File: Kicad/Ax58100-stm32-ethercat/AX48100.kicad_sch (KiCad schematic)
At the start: 33 parts, among them U2 AX58100, U3 24LC32A, Y1 NXK25.000AE12F-KAB6-12

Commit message: Steppers, encoders, IO, etc remapped
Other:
- title: (none) -> MetalMusings EaserCAT 3000
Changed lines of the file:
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@@
 (kicad_sch (version 20230121) (generator eeschema)
   (paper "A4")
+  (title_block
+    (title "MetalMusings EaserCAT 3000")
+  )
   (junction (at 236.22 125.73) (diameter 0) (color 0 0 0 0)
   )

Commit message: wip
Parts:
- renumbered C33 to C18, C31 to C19, C30 to C20, C29 to C21, C28 to C22, C27 to C23, C26 to C34, C25 to C35, C24 to C36, C23 to C37, C13 to C42, C18 to C43, C17 to C44, C16 to C45, C15 to C46, C14 to C47, C12 to C48, C11 to C49, R40 to R23, R39 to R24, R38 to R25, R37 to R26, R31 to R37, R30 to R38, R26 to R44, R25 to R45, R24 to R46, R23 to R47, R21 to R48, U2 to U11, U3 to U9, Y1 to Y2

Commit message: Might be in final shape.
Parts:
- renumbered C22 to C16, C34 to C20, C36 to C21, C18 to C22, C19 to C23, C20 to C24, C21 to C25, C23 to C27, C35 to C39, C37 to C40, C42 to C45, C43 to C46, C44 to C47, C45 to C48, C46 to C49, C47 to C50, C48 to C51, C49 to C52, R26 to R41, R38 to R42, R25 to R43, R24 to R44, R23 to R46, R37 to R57, R44 to R64, R45 to R65, R46 to R66, R47 to R67, R48 to R68, U11 to U10, U9 to U8

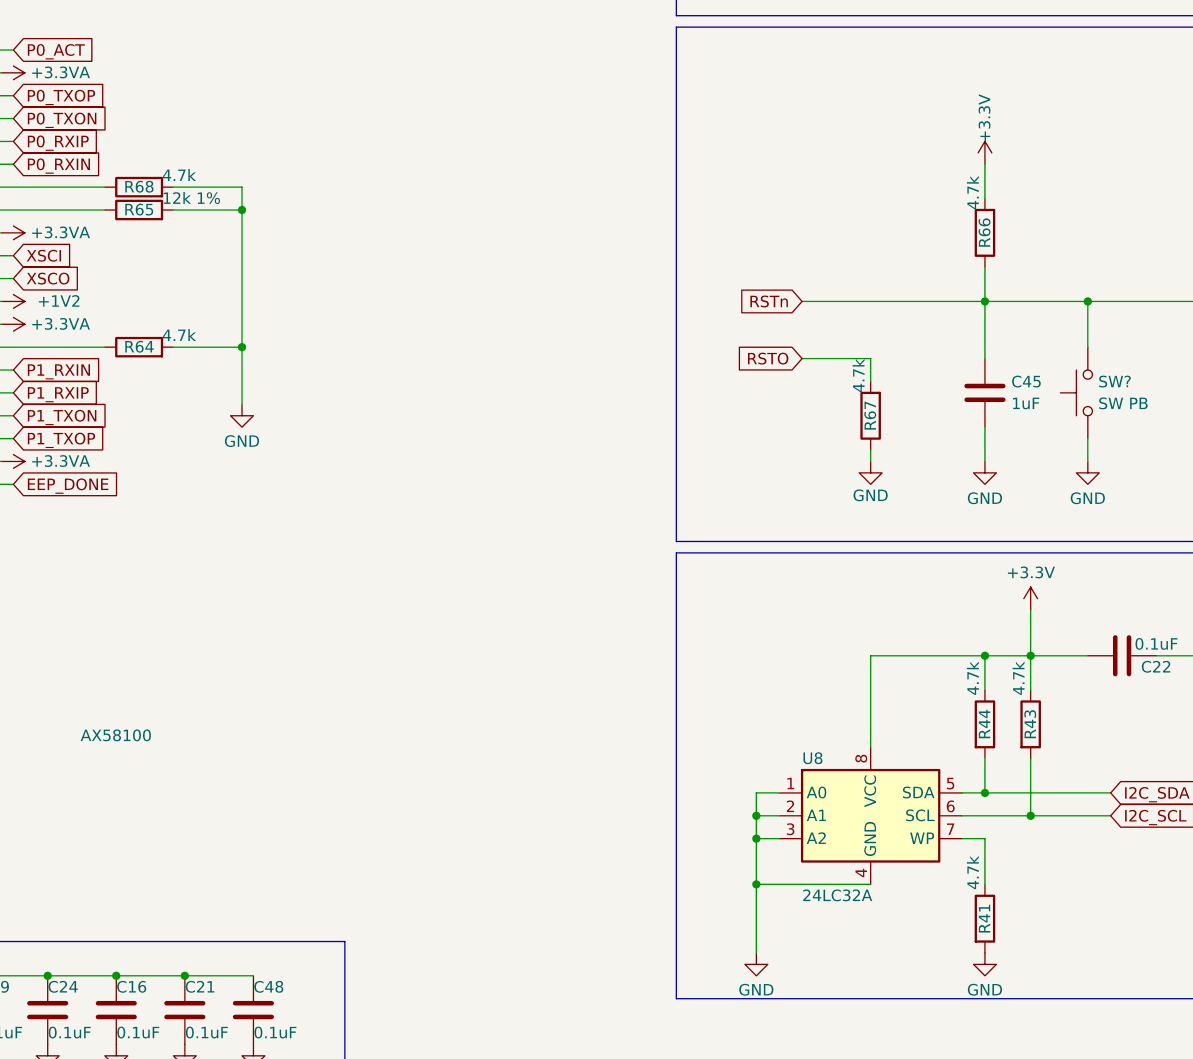
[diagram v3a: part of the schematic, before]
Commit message: 4.7k to 4k7
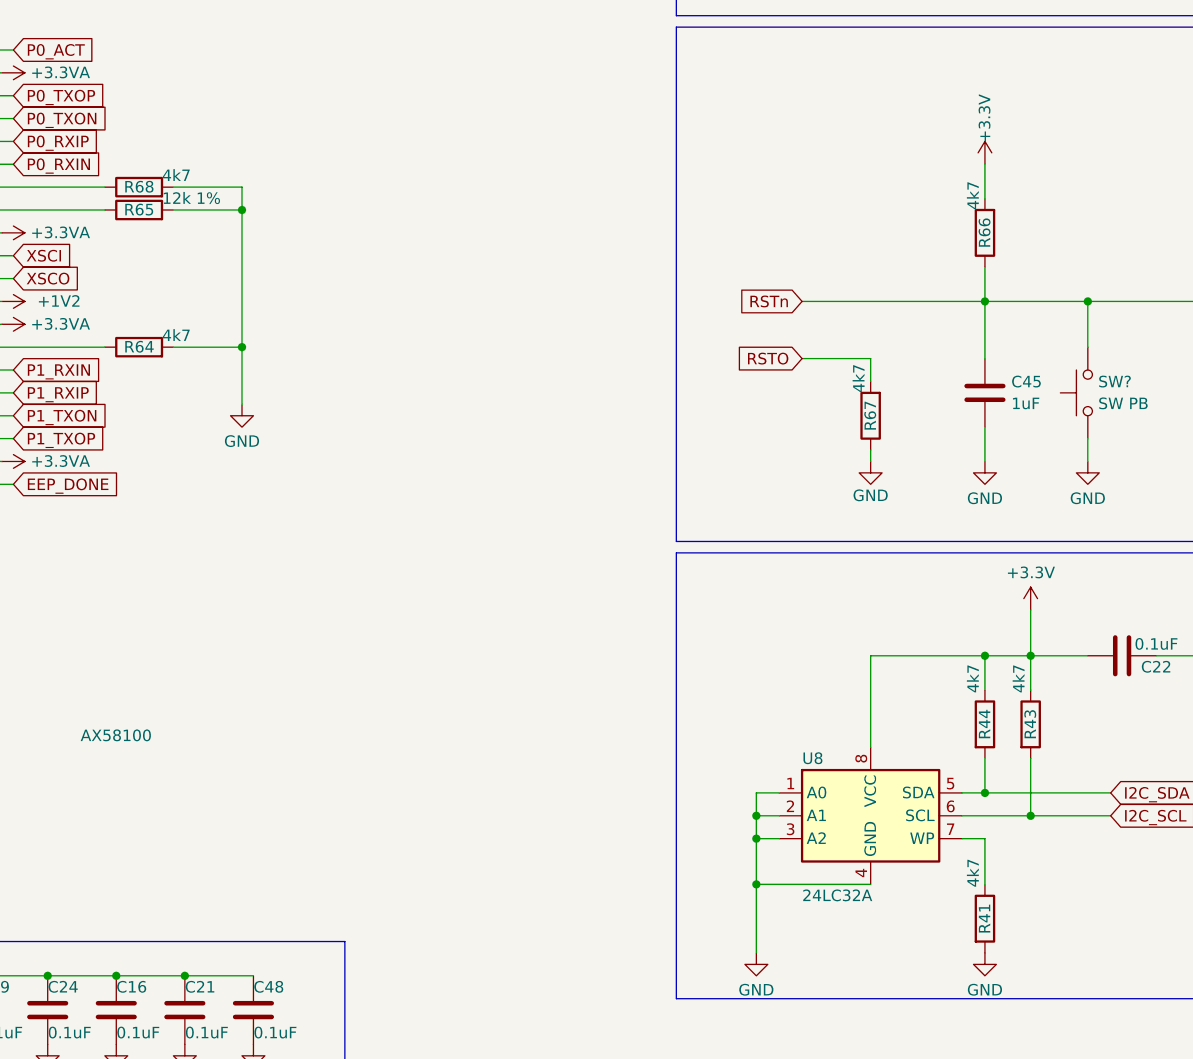
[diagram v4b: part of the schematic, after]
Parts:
- R41, R43, R44, R64, R66, R67, R68: value 4.7k -> 4k7
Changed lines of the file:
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@@
       (effects (font (size 1.27 1.27)))
     )
-    (property "Value" "4.7k" (at 234.95 76.2 90)
+    (property "Value" "4k7" (at 234.95 76.2 90)
       (effects (font (size 1.27 1.27)) (justify right))
     )
@@
       (effects (font (size 1.27 1.27)))
     )
-    (property "Value" "4.7k" (at 144.78 72.39 90)
+    (property "Value" "4k7" (at 144.78 72.39 90)
       (effects (font (size 1.27 1.27)) (justify right))
     )
@@
       (effects (font (size 1.27 1.27)))
     )
-    (property "Value" "4.7k" (at 144.78 90.17 90)
+    (property "Value" "4k7" (at 144.78 90.17 90)
       (effects (font (size 1.27 1.27)) (justify right))
     )
@@
       (effects (font (size 1.27 1.27)))
     )
-    (property "Value" "4.7k" (at 234.95 128.27 90)
+    (property "Value" "4k7" (at 234.95 128.27 90)
       (effects (font (size 1.27 1.27)))
     )
@@
       (effects (font (size 1.27 1.27)))
     )
-    (property "Value" "4.7k" (at 234.95 149.86 90)
+    (property "Value" "4k7" (at 234.95 149.86 90)
       (effects (font (size 1.27 1.27)))
     )
@@
       (effects (font (size 1.27 1.27)))
     )
-    (property "Value" "4.7k" (at 240.03 128.27 90)
+    (property "Value" "4k7" (at 240.03 128.27 90)
       (effects (font (size 1.27 1.27)))
     )
@@
       (effects (font (size 1.27 1.27)))
     )
-    (property "Value" "4.7k" (at 222.25 96.52 90)
+    (property "Value" "4k7" (at 222.25 96.52 90)
       (effects (font (size 1.27 1.27)) (justify right))
     )

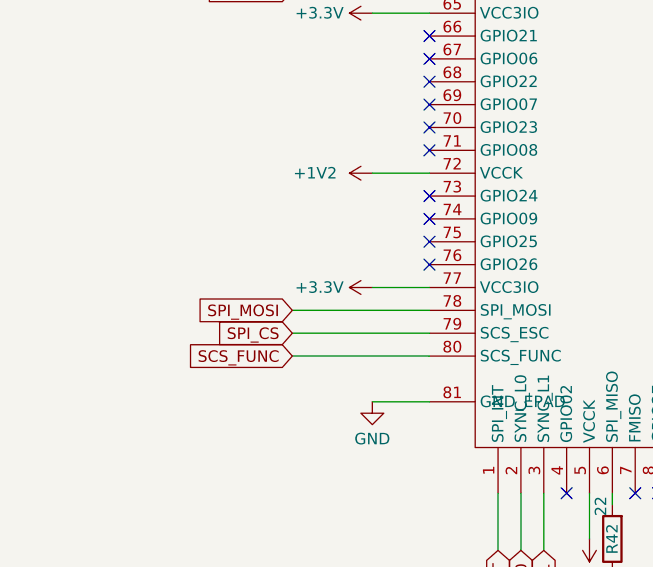
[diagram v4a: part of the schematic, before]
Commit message: Added 4k7 pullup onm scs_func. Think not needed since it is to a pin on stm32, but in case
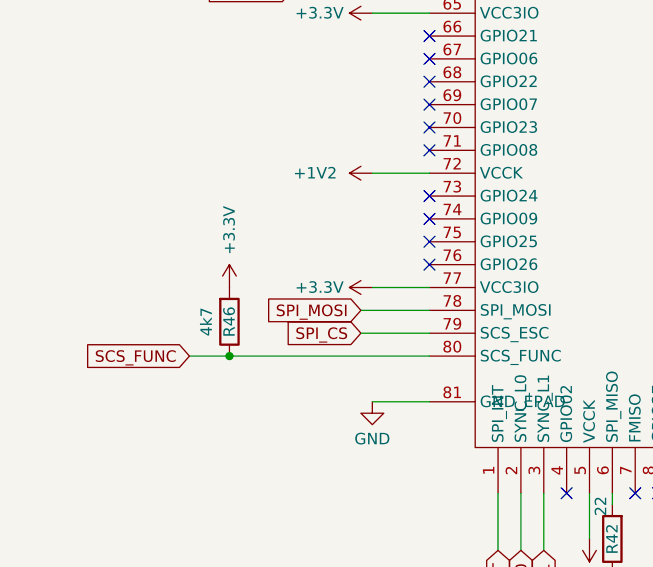
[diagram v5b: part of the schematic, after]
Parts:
- added R46: 4k7, Resistor_SMD:R_0603_1608Metric, symbol Device:R
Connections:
- net +3.3V: now also R46.2
- net SCS_FUNC: now also R46.1
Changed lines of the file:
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@@
   (junction (at 153.67 76.2) (diameter 0) (color 0 0 0 0)
+  )
+  (junction (at 37.465 106.68) (diameter 0) (color 0 0 0 0)
   )
   (junction (at 241.3 125.73) (diameter 0) (color 0 0 0 0)
@@
     (stroke (width 0) (type default))
   )
-  (wire (pts (xy 44.45 106.68) (xy 59.69 106.68))
-    (stroke (width 0) (type default))
-  )
   (wire (pts (xy 44.45 66.04) (xy 59.69 66.04))
     (stroke (width 0) (type default))
@@
     (stroke (width 0) (type default))
   )
-  (wire (pts (xy 44.45 101.6) (xy 59.69 101.6))
+  (wire (pts (xy 52.07 101.6) (xy 59.69 101.6))
     (stroke (width 0) (type default))
   )
@@
     (stroke (width 0) (type default))
   )
-  (wire (pts (xy 44.45 104.14) (xy 59.69 104.14))
+  (wire (pts (xy 52.07 104.14) (xy 59.69 104.14))
     (stroke (width 0) (type default))
   )
@@
     (stroke (width 0) (type default))
   )
+  (wire (pts (xy 33.02 106.68) (xy 37.465 106.68))
+    (stroke (width 0) (type default))
+  )
   (wire (pts (xy 128.27 81.28) (xy 121.92 81.28))
     (stroke (width 0) (type default))
@@
     (stroke (width 0) (type default))
   )
+  (wire (pts (xy 37.465 106.68) (xy 59.69 106.68))
+    (stroke (width 0) (type default))
+  )
   (wire (pts (xy 53.34 86.36) (xy 59.69 86.36))
     (stroke (width 0) (type default))
@@
     )
   )
-  (global_label "SPI_MOSI" (shape input) (at 44.45 101.6 180) (fields_autoplaced)
-    (effects (font (size 1.27 1.27)) (justify right))
-    (property "Intersheetrefs" "${INTERSHEET_REFS}" (at 32.8167 101.6 0)
+  (global_label "SPI_MOSI" (shape input) (at 52.07 101.6 180) (fields_autoplaced)
+    (effects (font (size 1.27 1.27)) (justify right))
+    (property "Intersheetrefs" "${INTERSHEET_REFS}" (at 40.4367 101.6 0)
       (effects (font (size 1.27 1.27)) (justify right) hide)
     )
@@
     )
   )
-  (global_label "SCS_FUNC" (shape input) (at 44.45 106.68 180) (fields_autoplaced)
-    (effects (font (size 1.27 1.27)) (justify right))
-    (property "Intersheetrefs" "${INTERSHEET_REFS}" (at 31.7886 106.68 0)
+  (global_label "SCS_FUNC" (shape input) (at 33.02 106.68 180) (fields_autoplaced)
+    (effects (font (size 1.27 1.27)) (justify right))
+    (property "Intersheetrefs" "${INTERSHEET_REFS}" (at 20.3586 106.68 0)
       (effects (font (size 1.27 1.27)) (justify right) hide)
     )
@@
     )
   )
-  (global_label "SPI_CS" (shape input) (at 44.45 104.14 180) (fields_autoplaced)
-    (effects (font (size 1.27 1.27)) (justify right))
-    (property "Intersheetrefs" "${INTERSHEET_REFS}" (at 34.9334 104.14 0)
+  (global_label "SPI_CS" (shape input) (at 52.07 104.14 180) (fields_autoplaced)
+    (effects (font (size 1.27 1.27)) (justify right))
+    (property "Intersheetrefs" "${INTERSHEET_REFS}" (at 42.5534 104.14 0)
       (effects (font (size 1.27 1.27)) (justify right) hide)
     )
@@
     )
   )
+  (symbol (lib_id "Device:R") (at 37.465 102.87 0) (mirror x) (unit 1)
+    (in_bom yes) (on_board yes) (dnp no)
+    (property "Reference" "R46" (at 37.465 102.87 90)
+      (effects (font (size 1.27 1.27)))
+    )
+    (property "Value" "4k7" (at 34.925 102.87 90)
+      (effects (font (size 1.27 1.27)))
+    )
+    (property "Footprint" "Resistor_SMD:R_0603_1608Metric" (at 35.687 102.87 90)
+      (effects (font (size 1.27 1.27)) hide)
+    )
+    (property "Datasheet" "~" (at 37.465 102.87 0)
+      (effects (font (size 1.27 1.27)) hide)
+    )
+    (pin "1")
+    (pin "2")
+    (instances
+      (project "Ax58100-stm32-ethercat"
+        (path "/5597aedc-b607-407f-bbfd-31b3b298ecb1/d564400f-40ba-4aca-9c2a-14ec52a8353b"
+          (reference "R46") (unit 1)
+        )
+        (path "/5597aedc-b607-407f-bbfd-31b3b298ecb1/0a376a6c-0f15-42f8-81f6-3a55619be267"
+          (reference "R2") (unit 1)
+        )
+        (path "/5597aedc-b607-407f-bbfd-31b3b298ecb1/9f485422-734f-43d3-94ea-443cbc453d2e"
+          (reference "R71") (unit 1)
+        )
+      )
+    )
+  )
   (symbol (lib_id "power:GND") (at 147.32 168.91 0) (unit 1)
     (in_bom yes) (on_board yes) (dnp no) (fields_autoplaced)
@@
         )
       )
+    )
+  )
+  (symbol (lib_id "power:+3.3V") (at 37.465 99.06 0) (unit 1)
+    (in_bom yes) (on_board yes) (dnp no)
+    (property "Reference" "#PWR0122" (at 37.465 102.87 0)
+      (effects (font (size 1.27 1.27)) hide)
+    )
+    (property "Value" "+3.3V" (at 37.465 92.71 90)
+      (effects (font (size 1.27 1.27)))
+    )
+    (property "Footprint" "" (at 37.465 99.06 0)
+      (effects (font (size 1.27 1.27)) hide)
+    )
+    (property "Datasheet" "" (at 37.465 99.06 0)
+      (effects (font (size 1.27 1.27)) hide)
+    )
+    (pin "1")
+    (instances
+      (project "Ax58100-stm32-ethercat"
+        (path "/5597aedc-b607-407f-bbfd-31b3b298ecb1/9f485422-734f-43d3-94ea-443cbc453d2e"
+          (reference "#PWR0122") (unit 1)
+        )
+      )

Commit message: Getting ready for fab
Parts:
- renumbered R42 to R43, R43 to R44, R44 to R45, R46 to R47, R57 to R58, R64 to R65, R65 to R66, R66 to R67, R67 to R68, R68 to R69
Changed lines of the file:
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@@
         )
         (path "/5597aedc-b607-407f-bbfd-31b3b298ecb1/9f485422-734f-43d3-94ea-443cbc453d2e"
-          (reference "R71") (unit 1)
+          (reference "R42") (unit 1)
         )
       )
@@
   (symbol (lib_id "Device:R") (at 80.01 127 180) (unit 1)
     (in_bom yes) (on_board yes) (dnp no)
-    (property "Reference" "R42" (at 80.01 127 90)
+    (property "Reference" "R43" (at 80.01 127 90)
       (effects (font (size 1.27 1.27)))
     )
@@
       (project "Ax58100-stm32-ethercat"
         (path "/5597aedc-b607-407f-bbfd-31b3b298ecb1/9f485422-734f-43d3-94ea-443cbc453d2e"
-          (reference "R42") (unit 1)
+          (reference "R43") (unit 1)
         )
       )
@@
   (symbol (lib_id "Device:R") (at 52.07 60.96 90) (unit 1)
     (in_bom yes) (on_board yes) (dnp no)
-    (property "Reference" "R46" (at 52.07 60.96 90)
+    (property "Reference" "R47" (at 52.07 60.96 90)
       (effects (font (size 1.27 1.27)))
     )
@@
       (project "Ax58100-stm32-ethercat"
         (path "/5597aedc-b607-407f-bbfd-31b3b298ecb1/9f485422-734f-43d3-94ea-443cbc453d2e"
-          (reference "R46") (unit 1)
+          (reference "R47") (unit 1)
         )
       )
@@
   (symbol (lib_id "Device:R") (at 236.22 78.74 180) (unit 1)
     (in_bom yes) (on_board yes) (dnp no)
-    (property "Reference" "R66" (at 236.22 78.74 90)
+    (property "Reference" "R67" (at 236.22 78.74 90)
       (effects (font (size 1.27 1.27)))
     )
@@
       (project "Ax58100-stm32-ethercat"
         (path "/5597aedc-b607-407f-bbfd-31b3b298ecb1/9f485422-734f-43d3-94ea-443cbc453d2e"
-          (reference "R66") (unit 1)
+          (reference "R67") (unit 1)
         )
       )
@@
   (symbol (lib_id "Device:R") (at 142.24 73.66 90) (unit 1)
     (in_bom yes) (on_board yes) (dnp no)
-    (property "Reference" "R68" (at 142.24 73.66 90)
+    (property "Reference" "R69" (at 142.24 73.66 90)
       (effects (font (size 1.27 1.27)))
     )
@@
       (project "Ax58100-stm32-ethercat"
         (path "/5597aedc-b607-407f-bbfd-31b3b298ecb1/9f485422-734f-43d3-94ea-443cbc453d2e"
-          (reference "R68") (unit 1)
+          (reference "R69") (unit 1)
         )
       )
@@
   (symbol (lib_id "Device:R") (at 142.24 91.44 90) (unit 1)
     (in_bom yes) (on_board yes) (dnp no)
-    (property "Reference" "R64" (at 142.24 91.44 90)
+    (property "Reference" "R65" (at 142.24 91.44 90)
       (effects (font (size 1.27 1.27)))
     )
@@
       (project "Ax58100-stm32-ethercat"
         (path "/5597aedc-b607-407f-bbfd-31b3b298ecb1/9f485422-734f-43d3-94ea-443cbc453d2e"
-          (reference "R64") (unit 1)
+          (reference "R65") (unit 1)
         )
       )
@@
   (symbol (lib_id "Device:R") (at 236.22 133.35 0) (unit 1)
     (in_bom yes) (on_board yes) (dnp no)
-    (property "Reference" "R44" (at 236.22 133.35 90)
+    (property "Reference" "R45" (at 236.22 133.35 90)
       (effects (font (size 1.27 1.27)))
     )
@@
       (project "Ax58100-stm32-ethercat"
         (path "/5597aedc-b607-407f-bbfd-31b3b298ecb1/9f485422-734f-43d3-94ea-443cbc453d2e"
-          (reference "R44") (unit 1)
+          (reference "R45") (unit 1)
         )
       )
@@
   (symbol (lib_id "Device:R") (at 142.24 76.2 90) (unit 1)
     (in_bom yes) (on_board yes) (dnp no)
-    (property "Reference" "R65" (at 142.24 76.2 90)
+    (property "Reference" "R66" (at 142.24 76.2 90)
       (effects (font (size 1.27 1.27)))
     )
@@
       (project "Ax58100-stm32-ethercat"
         (path "/5597aedc-b607-407f-bbfd-31b3b298ecb1/9f485422-734f-43d3-94ea-443cbc453d2e"
-          (reference "R65") (unit 1)
+          (reference "R66") (unit 1)
         )
       )
@@
   (symbol (lib_id "Device:R") (at 69.85 36.83 180) (unit 1)
     (in_bom yes) (on_board yes) (dnp no)
-    (property "Reference" "R57" (at 69.85 36.83 90)
+    (property "Reference" "R58" (at 69.85 36.83 90)
       (effects (font (size 1.27 1.27)))
     )
@@
       (project "Ax58100-stm32-ethercat"
         (path "/5597aedc-b607-407f-bbfd-31b3b298ecb1/9f485422-734f-43d3-94ea-443cbc453d2e"
-          (reference "R57") (unit 1)
+          (reference "R58") (unit 1)
         )
       )
@@
   (symbol (lib_id "Device:R") (at 241.3 133.35 0) (unit 1)
     (in_bom yes) (on_board yes) (dnp no)
-    (property "Reference" "R43" (at 241.3 133.35 90)
+    (property "Reference" "R44" (at 241.3 133.35 90)
       (effects (font (size 1.27 1.27)))
     )
@@
       (project "Ax58100-stm32-ethercat"
         (path "/5597aedc-b607-407f-bbfd-31b3b298ecb1/9f485422-734f-43d3-94ea-443cbc453d2e"
-          (reference "R43") (unit 1)
+          (reference "R44") (unit 1)
         )
       )
@@
   (symbol (lib_id "Device:R") (at 223.52 99.06 180) (unit 1)
     (in_bom yes) (on_board yes) (dnp no)
-    (property "Reference" "R67" (at 223.52 99.06 90)
+    (property "Reference" "R68" (at 223.52 99.06 90)
       (effects (font (size 1.27 1.27)))
     )
@@
       (project "Ax58100-stm32-ethercat"
         (path "/5597aedc-b607-407f-bbfd-31b3b298ecb1/9f485422-734f-43d3-94ea-443cbc453d2e"
-          (reference "R67") (unit 1)
-        )
-      )
+          (reference "R68") (unit 1)
+        )
+      )
